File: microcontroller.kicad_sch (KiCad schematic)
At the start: 0 parts

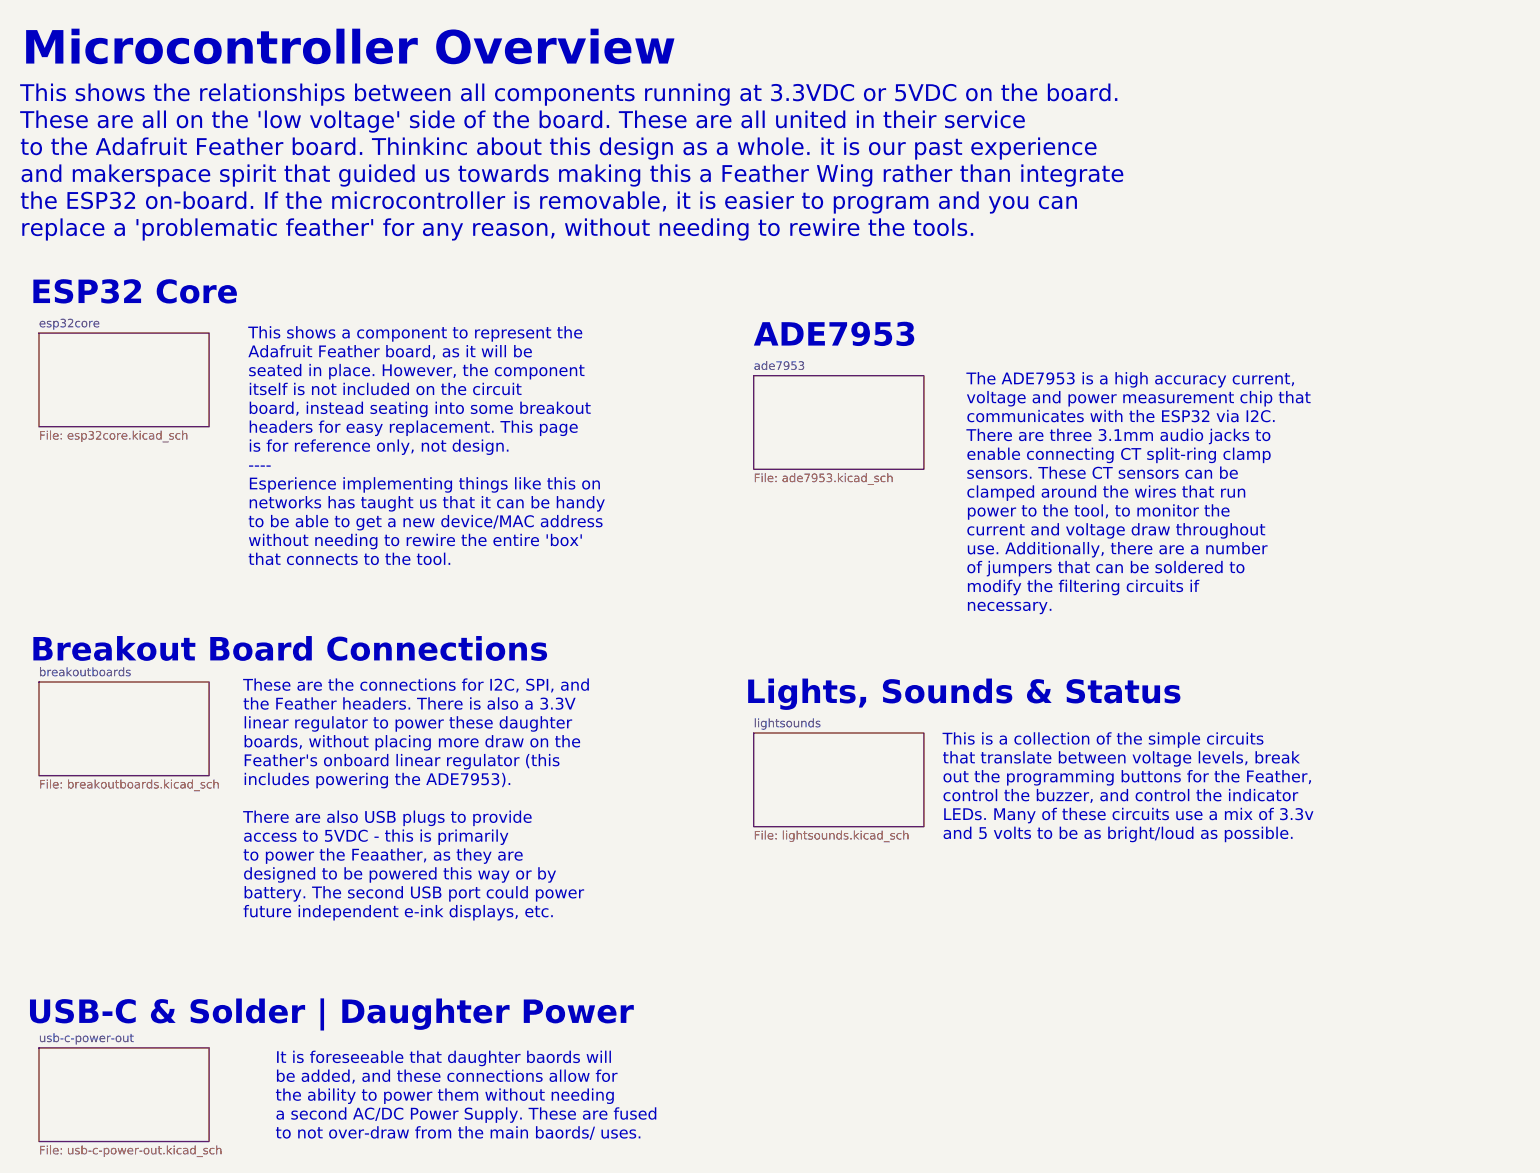
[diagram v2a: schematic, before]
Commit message: 5v binary current and cleanup
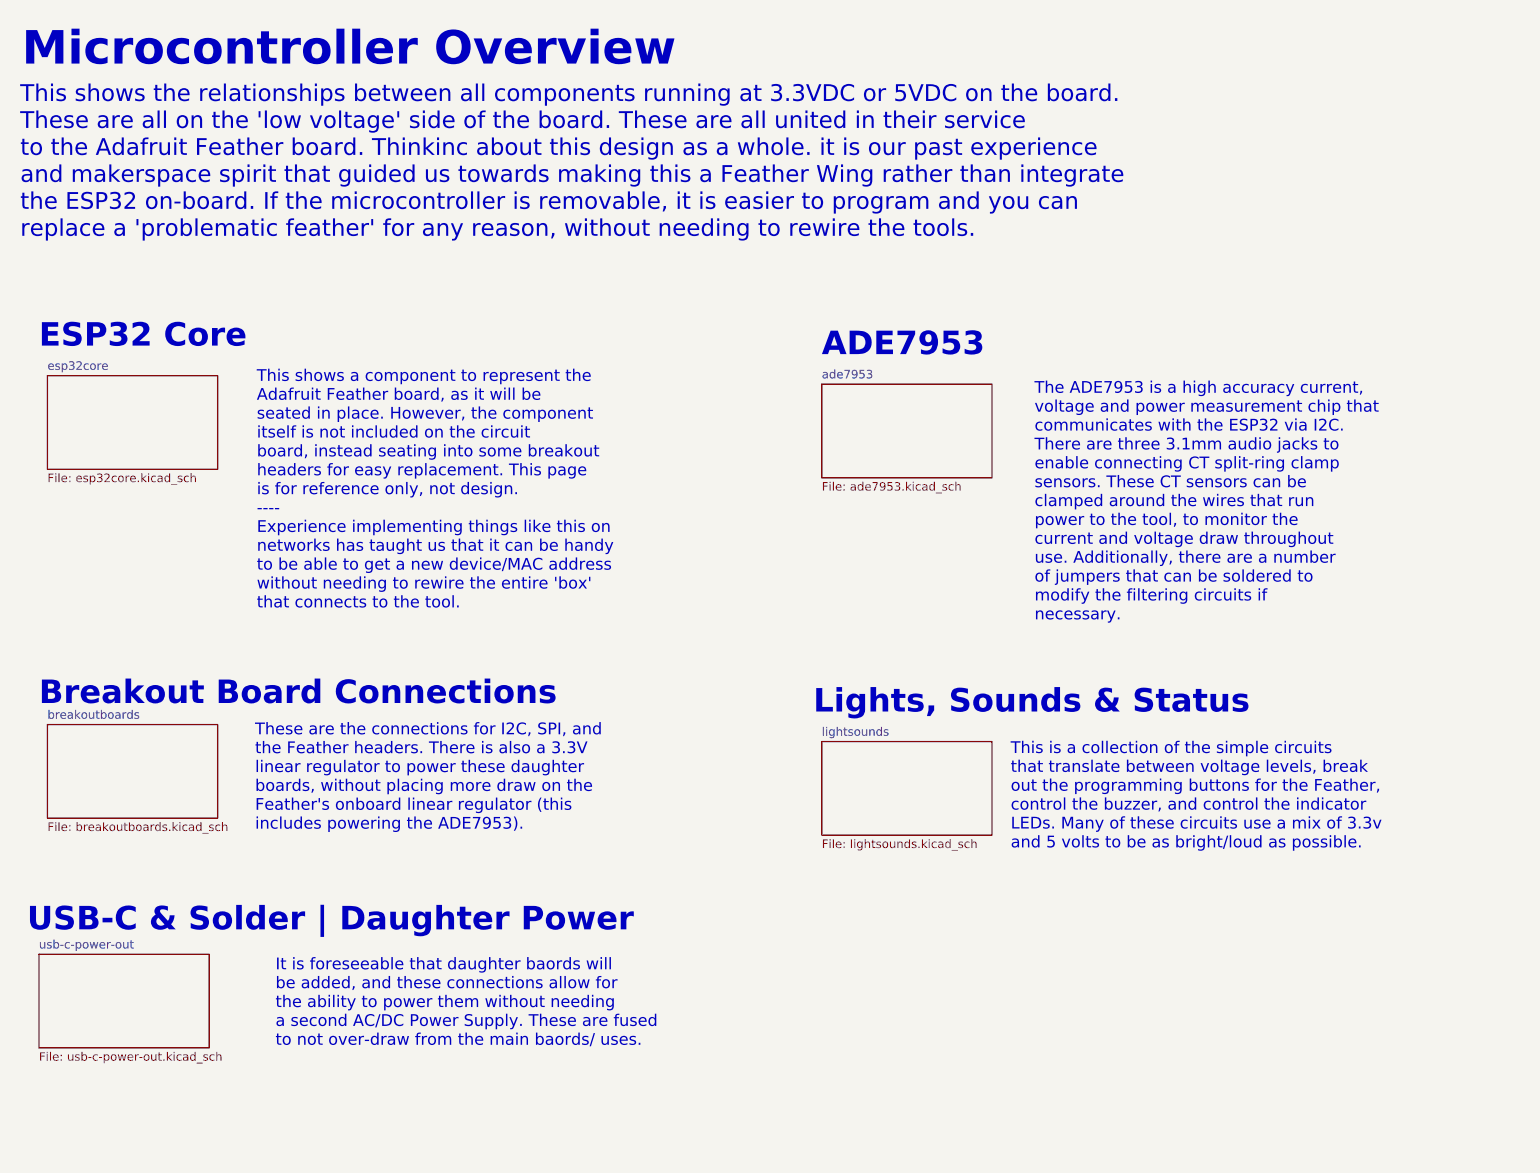
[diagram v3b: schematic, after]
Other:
- note added: "These are the connections for I2C, SPI, and the Feather headers. There is also a 3.3V linear regulator to power these daughter boards, without placing more draw on the Feather's onboard linear regulator (this includes powering the ADE7953)."
- note added: "This shows a component to represent the Adafruit Feather board, as it will be seated in place. However, the component itself is not included on the circuit board, instead seating into some breakout headers for easy replacement. This page is for reference only, not design. ---- Experience implementing things like this on networks has taught us that it can be handy to be able to get a new device/MA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"
- note removed: "These are the connections for I2C, SPI, and the Feather headers. There is also a 3.3V linear regulator to power these daughter boards, without placing more draw on the Feather's onboard linear regulator (this includes powering the ADE7953). There are also USB plugs to provide access to 5VDC - this is primarily to power the Feaather, as they are designed to be powered this way or by battery. The s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"
- note removed: "This shows a component to represent the Adafruit Feather board, as it will be seated in place. However, the component itself is not included on the circuit board, instead seating into some breakout headers for easy replacement. This page is for reference only, not design. ---- Esperience implementing things like this on networks has taught us that it can be handy to be able to get a new device/MA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"
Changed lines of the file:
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@@
 	(text "This is a collection of the simple circuits \nthat translate between voltage levels, break \nout the programming buttons for the Feather, \ncontrol the buzzer, and control the indicator \nLEDs. Many of these circuits use a mix of 3.3v\nand 5 volts to be as bright/loud as possible.\n"
 		(exclude_from_sim no)
-		(at 171.704 147.066 0)
-		(effects
-			(font
-				(size 1.75 1.75)
-			)
-			(justify left bottom)
-		)
-	)
-	(text "This shows a component to represent the \nAdafruit Feather board, as it will be \nseated in place. However, the component \nitself is not included on the circuit \nboard, instead seating into some breakout \nheaders for easy replacement. This page \nis for reference only, not design.\n----\nEsperience implementing things like this on \nnetworks has taught us that it can be handy\nto be able to get a new device/MAC address \nwithout needing to rewire the entire 'box'\nthat connects to the tool."
-		(exclude_from_sim no)
-		(at 68.072 106.172 0)
+		(at 181.864 148.336 0)
+		(effects
+			(font
+				(size 1.75 1.75)
+			)
+			(justify left bottom)
+		)
+	)
+	(text "This shows a component to represent the \nAdafruit Feather board, as it will be \nseated in place. However, the component \nitself is not included on the circuit \nboard, instead seating into some breakout \nheaders for easy replacement. This page \nis for reference only, not design.\n----\nExperience implementing things like this on \nnetworks has taught us that it can be handy\nto be able to get a new device/MAC address \nwithout needing to rewire the entire 'box'\nthat connects to the tool."
+		(exclude_from_sim no)
+		(at 69.342 112.522 0)
 		(effects
 			(font
@@
 	(text "Breakout Board Connections"
 		(exclude_from_sim no)
-		(at 35.56 120.65 0)
-		(effects
-			(font
-				(size 3.5 3.5)
-				(bold yes)
-			)
-			(justify left bottom)
-		)
-	)
-	(text "These are the connections for I2C, SPI, and \nthe Feather headers. There is also a 3.3V \nlinear regulator to power these daughter \nboards, without placing more draw on the \nFeather's onboard linear regulator (this \nincludes powering the ADE7953).\n\nThere are also USB plugs to provide \naccess to 5VDC - this is primarily \nto power the Feaather, as they are \ndesigned to be powered this way or by\nbattery. The second USB port could power \nfuture independent e-ink displays, etc.\n"
-		(exclude_from_sim no)
-		(at 67.31 158.75 0)
+		(at 36.83 127 0)
+		(effects
+			(font
+				(size 3.5 3.5)
+				(bold yes)
+			)
+			(justify left bottom)
+		)
+	)
+	(text "These are the connections for I2C, SPI, and \nthe Feather headers. There is also a 3.3V \nlinear regulator to power these daughter \nboards, without placing more draw on the \nFeather's onboard linear regulator (this \nincludes powering the ADE7953)."
+		(exclude_from_sim no)
+		(at 69.088 145.542 0)
 		(effects
 			(font
@@
 	(text "Lights, Sounds & Status"
 		(exclude_from_sim no)
-		(at 142.24 127 0)
+		(at 152.4 128.27 0)
 		(effects
 			(font
@@
 	(text "The ADE7953 is a high accuracy current, \nvoltage and power measurement chip that \ncommunicates with the ESP32 via I2C. \nThere are three 3.1mm audio jacks to \nenable connecting CT split-ring clamp \nsensors. These CT sensors can be \nclamped around the wires that run \npower to the tool, to monitor the \ncurrent and voltage draw throughout \nuse. Additionally, there are a number \nof jumpers that can be soldered to \nmodify the filtering circuits if \nnecessary. "
 		(exclude_from_sim no)
-		(at 175.26 113.03 0)
+		(at 185.42 114.3 0)
 		(effects
 			(font
@@
 	(text "ESP32 Core"
 		(exclude_from_sim no)
-		(at 35.56 67.31 0)
+		(at 36.83 73.66 0)
 		(effects
 			(font
@@
 	(text "USB-C & Solder | Daughter Power"
 		(exclude_from_sim no)
-		(at 35.052 174.752 0)
+		(at 35.052 160.782 0)
 		(effects
 			(font
@@
 	(text "It is foreseeable that daughter baords will \nbe added, and these connections allow for \nthe ability to power them without needing\na second AC/DC Power Supply. These are fused\nto not over-draw from the main baords/ uses."
 		(exclude_from_sim no)
-		(at 72.136 191.77 0)
+		(at 72.136 177.8 0)
 		(effects
 			(font
@@
 	(text "ADE7953"
 		(exclude_from_sim no)
-		(at 143.51 73.66 0)
-		(effects
-			(font
-				(size 3.5 3.5)
-				(bold yes)
-			)
-			(justify left bottom)
-		)
-	)
-	(sheet
-		(at 143.51 77.47)
+		(at 153.67 74.93 0)
+		(effects
+			(font
+				(size 3.5 3.5)
+				(bold yes)
+			)
+			(justify left bottom)
+		)
+	)
+	(sheet
+		(at 153.67 78.74)
 		(size 25.4 13.97)
 		(fields_autoplaced yes)
@@
 		)
 		(property "Sheetname" "ade7953"
-			(at 143.51 76.7584 0)
+			(at 153.67 78.0284 0)
 			(effects
 				(font
@@
 		)
 		(property "Sheetfile" "ade7953.kicad_sch"
-			(at 143.51 92.0246 0)
+			(at 153.67 93.2946 0)
 			(effects
 				(font
@@
 	)
 	(sheet
-		(at 36.83 71.12)
+		(at 38.1 77.47)
 		(size 25.4 13.97)
 		(fields_autoplaced yes)
@@
 		)
 		(property "Sheetname" "esp32core"
-			(at 36.83 70.4084 0)
+			(at 38.1 76.7584 0)
 			(effects
 				(font
@@
 		)
 		(property "Sheetfile" "esp32core.kicad_sch"
-			(at 36.83 85.6746 0)
+			(at 38.1 92.0246 0)
 			(effects
 				(font
@@
 	)
 	(sheet
-		(at 36.83 123.19)
+		(at 38.1 129.54)
 		(size 25.4 13.97)
 		(fields_autoplaced yes)
@@
 		)
 		(property "Sheetname" "breakoutboards"
-			(at 36.83 122.4784 0)
+			(at 38.1 128.8284 0)
 			(effects
 				(font
@@
 		)
 		(property "Sheetfile" "breakoutboards.kicad_sch"
-			(at 36.83 137.7446 0)
+			(at 38.1 144.0946 0)
 			(effects
 				(font
@@
 	)
 	(sheet
-		(at 36.83 177.8)
+		(at 36.83 163.83)
 		(size 25.4 13.97)
 		(fields_autoplaced yes)
@@
 		)
 		(property "Sheetname" "usb-c-power-out"
-			(at 36.83 177.0884 0)
+			(at 36.83 163.1184 0)
 			(effects
 				(font
@@
 		)
 		(property "Sheetfile" "usb-c-power-out.kicad_sch"
-			(at 36.83 192.3546 0)
-			(effects
-				(font
-					(size 1.27 1.27)
-				)
-				(justify left top)
-			)
-		)
-		(instances
-			(project "wing-combo"
-				(path "/586efc0f-7de2-49a7-ac21-ecfef2f716d6/3f0e9b91-fe15-47d5-84d6-aa71b368b91e"
-					(page "11")
-				)
-			)
-		)
-	)
-	(sheet
-		(at 143.51 130.81)
+			(at 36.83 178.3846 0)
+			(effects
+				(font
+					(size 1.27 1.27)
+				)
+				(justify left top)
+			)
+		)
+		(instances
+			(project "wing-combo"
+				(path "/586efc0f-7de2-49a7-ac21-ecfef2f716d6/3f0e9b91-fe15-47d5-84d6-aa71b368b91e"
+					(page "7")
+				)
+			)
+		)
+	)
+	(sheet
+		(at 153.67 132.08)
 		(size 25.4 13.97)
 		(fields_autoplaced yes)
@@
 		)
 		(property "Sheetname" "lightsounds"
-			(at 143.51 130.0984 0)
+			(at 153.67 131.3684 0)
 			(effects
 				(font
@@
 		)
 		(property "Sheetfile" "lightsounds.kicad_sch"
-			(at 143.51 145.3646 0)
-			(effects
-				(font
+			(at 153.67 146.6346 0)
+			(effects
+				(font

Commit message: close enough for 3D export
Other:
- note added: "This shows the relationships between all components running at 3.3VDC or 5VDC on the board. These are all on the 'low voltage' side of the board. These are all united in their service to the Adafruit Feather board. Thinking about this design as a whole, it is our past experience and makerspace spirit that guided us towards making this a Feather Wing rather than integrate the ESP32 on-board. If th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"
- note removed: "This shows the relationships between all components running at 3.3VDC or 5VDC on the board. These are all on the 'low voltage' side of the board. These are all united in their service to the Adafruit Feather board. Thinkinc about this design as a whole. it is our past experience and makerspace spirit that guided us towards making this a Feather Wing rather than integrate the ESP32 on-board. If th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"
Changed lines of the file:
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@@
 		(company "Corey Rice & MakeHaven")
 	)
-	(text "This shows the relationships between all components running at 3.3VDC or 5VDC on the board. \nThese are all on the 'low voltage' side of the board. These are all united in their service \nto the Adafruit Feather board. Thinkinc about this design as a whole. it is our past experience\nand makerspace spirit that guided us towards making this a Feather Wing rather than integrate\nthe ESP32 on-board. If the microcontroller is removable, it is easier to program and you can \nreplace a 'problematic feather' for any reason, without needing to rewire the tools. "
+	(text "This shows the relationships between all components running at 3.3VDC or 5VDC on the board. \nThese are all on the 'low voltage' side of the board. These are all united in their service \nto the Adafruit Feather board. Thinking about this design as a whole, it is our past experience\nand makerspace spirit that guided us towards making this a Feather Wing rather than integrate\nthe ESP32 on-board. If the microcontroller is removable, it is easier to program, and you can \nreplace a 'problematic feather' for any reason (without needing to rewire the tools). "
 		(exclude_from_sim no)
 		(at 34.036 57.15 0)
